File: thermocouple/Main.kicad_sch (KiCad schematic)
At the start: 17 parts, among them IC701 MCP9600, M701 BM15C, SW701 Join, X701 Debug, X702 Thermocouple

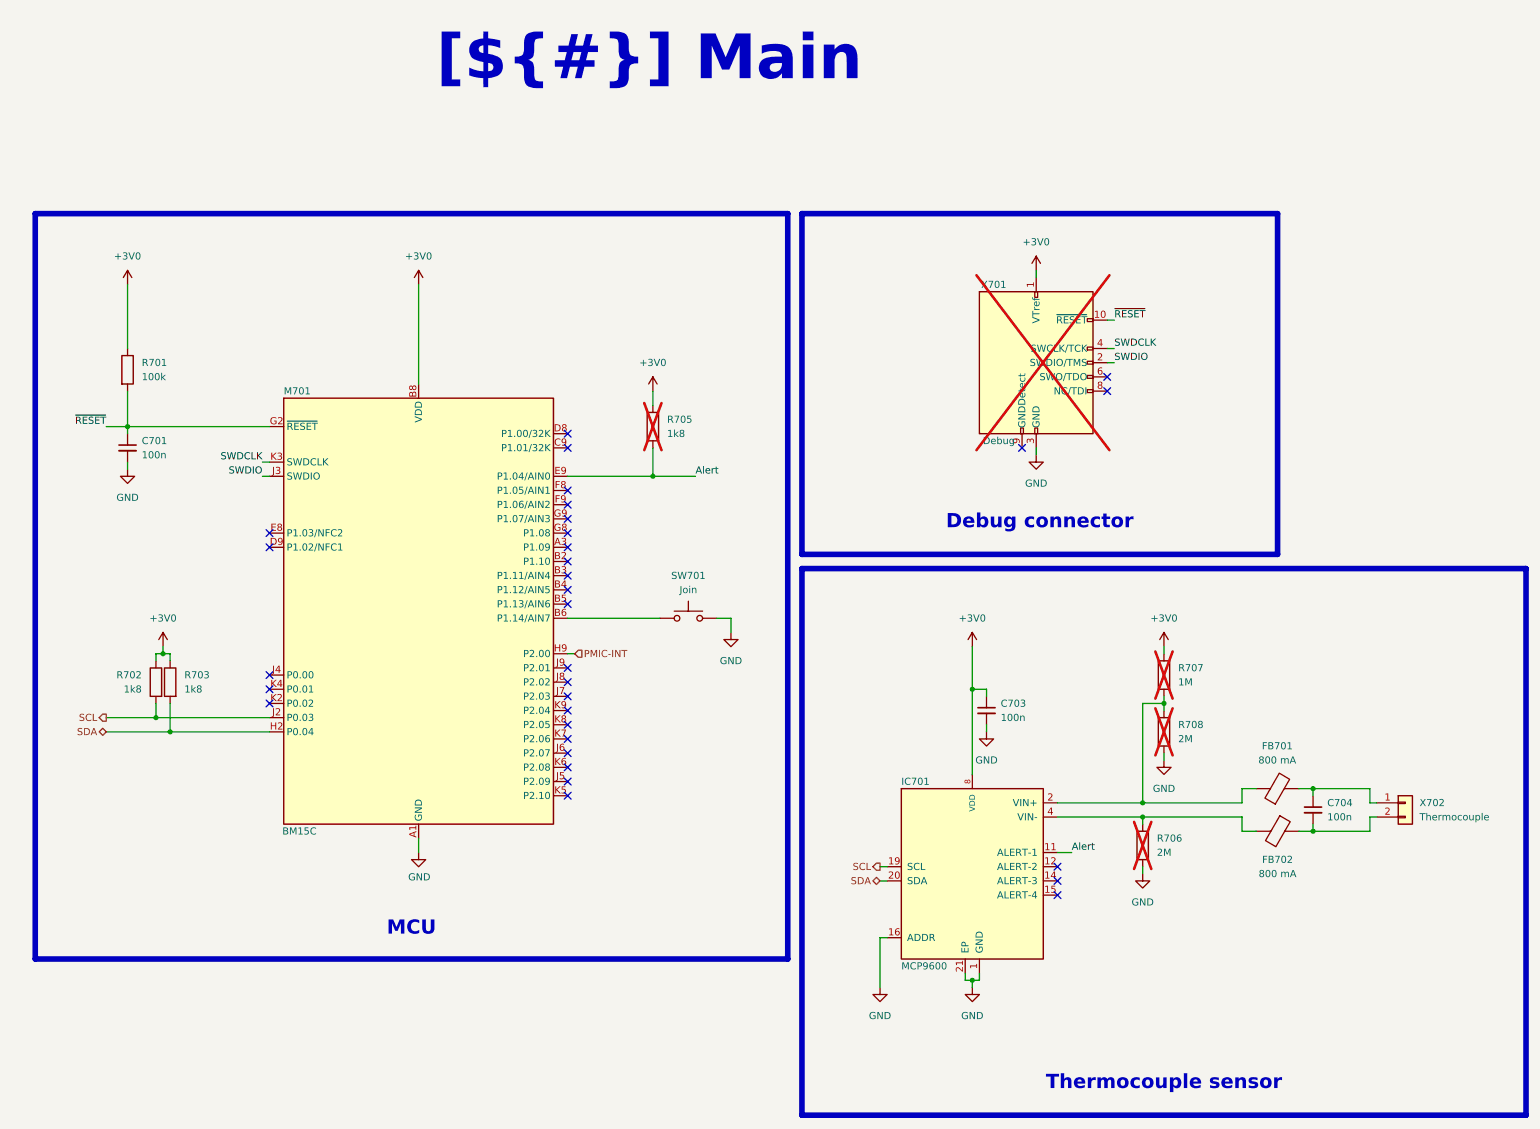
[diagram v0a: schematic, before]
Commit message: CI/CD improvements, fixing broken PMIC-INT
- Update CI/CD to the latest version
- Move PMIC-INT to port 0 to make it usable

Signed-off-by: Daniel Kampert <DanielKampert@kampis-elektroecke.de>
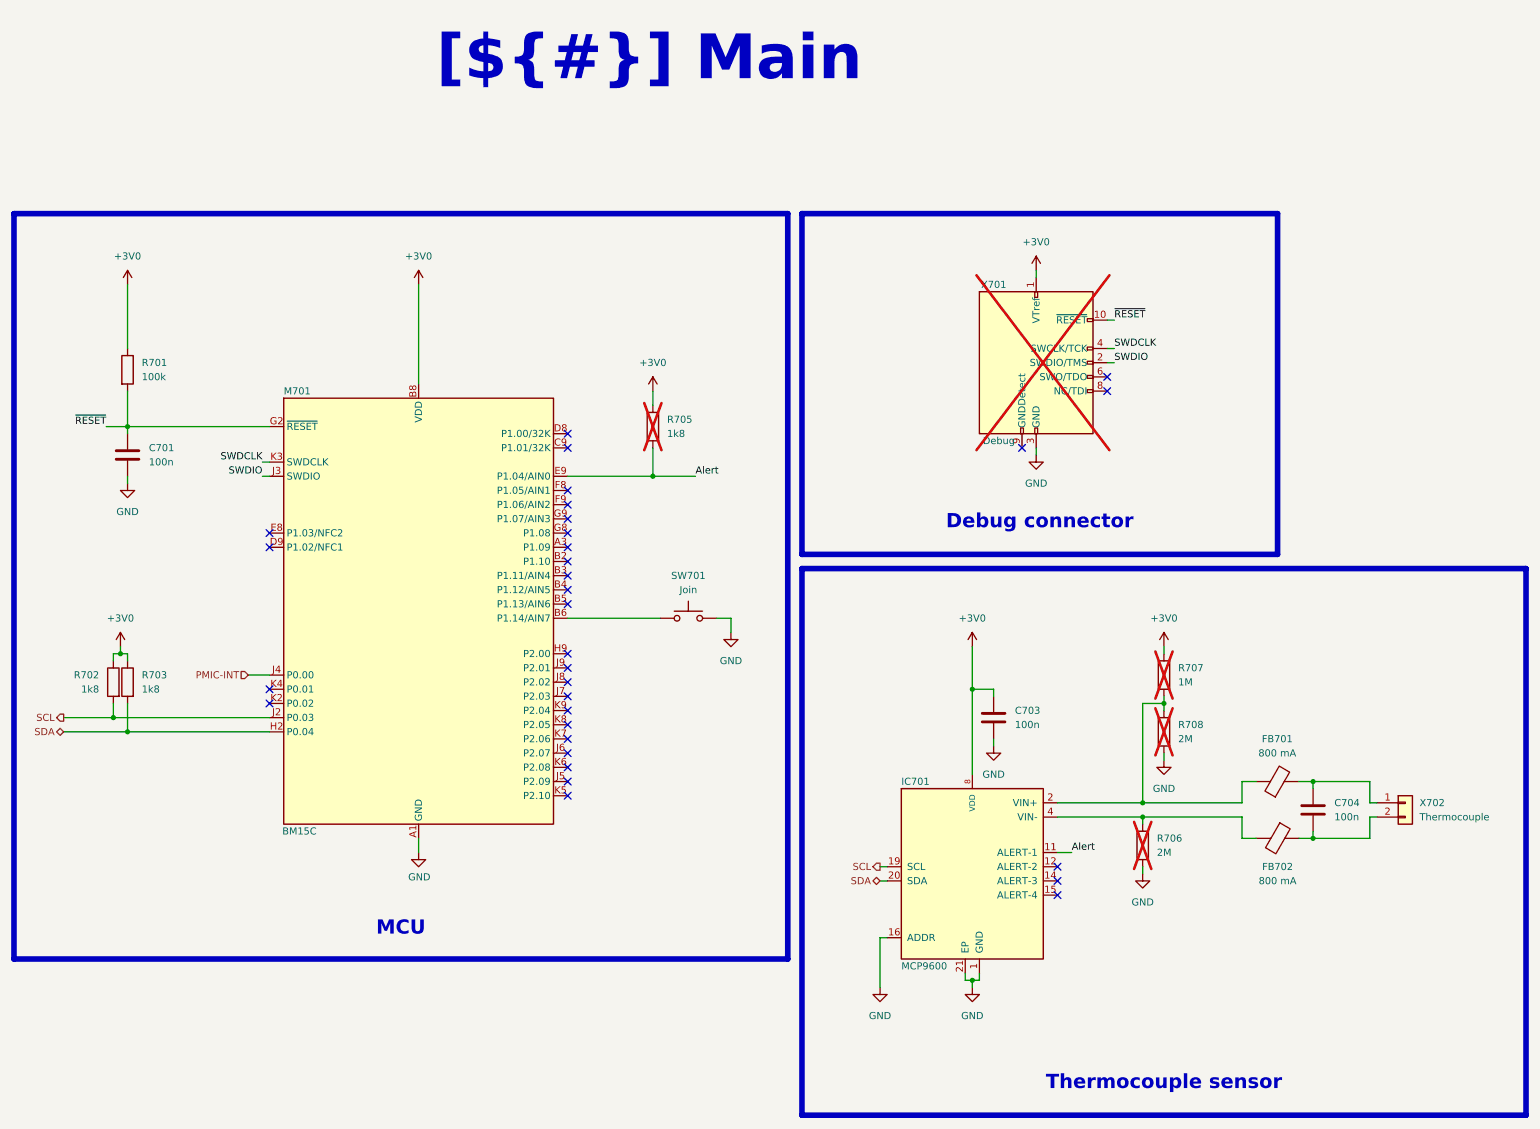
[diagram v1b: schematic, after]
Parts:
- C701, C703, C704: footprint Resistor_SMD:R_0805_2012Metric -> Capacitor_SMD:C_0805_2012Metric; symbol Device:C_Small -> partdb:08055C104K4Z4A; Category (none) -> Kondensator/MLCC; MPN (none) -> 08055C104K4Z4A; Manufacturer (none) -> KYOCERA AVX; Manufacturing Status (none) -> Active; Mass (none) -> 0.006 g; Mouser SPN (none) -> 581-08055C104K4Z4A; Part-DB Footprint (none) -> 0805; Part-DB ID (none) -> 109; Part-DB URL (none) -> https://inventory.lan/de/part/109/info; Stock (none) -> 6; Storage Location (none) -> Sortierregal; manf# 08053F104K4T2A -> 08055C104K4Z4A; mouser# 581-08053F104K4T2A -> 581-08055C104K4Z4A
- M701: symbol Fanstel:BM15C -> partdb:BM15C; Category (none) -> Modul/Fanstel; MPN (none) -> BM15C; Manufacturer (none) -> Fanstel; Manufacturing Status (none) -> Active; Mouser SPN (none) -> 308-BM15C; Part-DB Footprint (none) -> BM15C; Part-DB ID (none) -> 52; Part-DB URL (none) -> https://inventory.lan/de/part/52/info; Stock (none) -> 2; Storage Location (none) -> Sortierregal
- R701: symbol Device:R -> partdb:RT0805FRE13100KL; Category (none) -> Widerstand/Dünnfilmwiderstand; MPN (none) -> RT0805FRE13100KL; Manufacturer (none) -> YAGEO; Manufacturing Status (none) -> Active; Mass (none) -> 0.006 g; Mouser SPN (none) -> 603-RT0805FRE13100KL; Part-DB Footprint (none) -> 0805; Part-DB ID (none) -> 66; Part-DB URL (none) -> https://inventory.lan/de/part/66/info; Stock (none) -> 4; Storage Location (none) -> Sortierregal; manf Bourns -> YAGEO; manf# CR0805-JW-104ELF -> RT0805FRE13100KL; mouser# 652-CR0805-JW-104ELF -> 603-RT0805FRE13100KL
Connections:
- net PMIC-INT: now also M701.J4 (P0.00); no longer M701.H9 (P2.00)
- new net: IC701.10 (NC), IC701.13 (NC), IC701.17 (NC), IC701.18 (NC), IC701.3 (NC), IC701.5 (NC), IC701.6 (NC), IC701.7 (NC), IC701.9 (NC)
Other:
- moved on the sheet: C701, C703, FB701, FB702, R702, R703

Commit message: Change thermocouple connector to a different type
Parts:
- SW701: symbol Switch:SW_Push -> partdb:430182095816; Category (none) -> Bedienelement/Taster; MPN (none) -> 430182095816; Manufacturer (none) -> Wurth Elektronik; Manufacturing Status (none) -> Active; Mass (none) -> 0.26 g; Mouser SPN (none) -> 710-430182095816; Part-DB Footprint (none) -> WS-TASV 6x6; Part-DB ID (none) -> 24; Part-DB URL (none) -> https://inventory.lan/de/part/24/info; Stock (none) -> 0
- X702: footprint TerminalBlock_Phoenix:TerminalBlock_Phoenix_MKDS-1,5-2-5.08_1x02_P5.08mm_Horizontal -> Connector_Phoenix_MC:PhoenixContact_MC_1,5_2-G-3.81_1x02_P3.81mm_Horizontal; manf# 1729128 -> 1803277; mouser# 651-1729128 -> 651-1803277
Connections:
- net GND: now also SW701.4
- net at M701.B6 (P1.14/AIN7), SW701.1: now also SW701.3
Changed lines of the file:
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@@
 	)
 	(junction
+		(at 210.82 123.19)
+		(diameter 0)
+		(color 0 0 0 0)
+	)
+	(junction
 		(at 116.84 143.51)
 		(diameter 0)
@@
 	)
 	(junction
+		(at 224.79 123.19)
+		(diameter 0)
+		(color 0 0 0 0)
+	)
+	(junction
 		(at 328.93 152.4)
 		(diameter 0)
@@
 	(wire
 		(pts
+			(xy 210.82 120.65) (xy 210.82 123.19)
+		)
+		(stroke
+			(width 0)
+			(type default)
+		)
+	)
+	(wire
+		(pts
 			(xy 116.84 138.43) (xy 116.84 143.51)
 		)
@@
 	(wire
 		(pts
+			(xy 222.25 120.65) (xy 224.79 120.65)
+		)
+		(stroke
+			(width 0)
+			(type default)
+		)
+	)
+	(wire
+		(pts
 			(xy 116.84 97.79) (xy 116.84 99.06)
 		)
@@
 	(wire
 		(pts
+			(xy 210.82 123.19) (xy 212.09 123.19)
+		)
+		(stroke
+			(width 0)
+			(type default)
+		)
+	)
+	(wire
+		(pts
 			(xy 210.82 92.71) (xy 210.82 97.79)
 		)
@@
 	(wire
 		(pts
+			(xy 212.09 120.65) (xy 210.82 120.65)
+		)
+		(stroke
+			(width 0)
+			(type default)
+		)
+	)
+	(wire
+		(pts
 			(xy 218.44 97.79) (xy 210.82 97.79)
 		)
@@
 	(wire
 		(pts
-			(xy 195.58 123.19) (xy 212.09 123.19)
+			(xy 195.58 123.19) (xy 210.82 123.19)
 		)
 		(stroke
@@
 		)
 	)
+	(wire
+		(pts
+			(xy 224.79 120.65) (xy 224.79 123.19)
+		)
+		(stroke
+			(width 0)
+			(type default)
+		)
+	)
 	(label "Alert"
 		(at 218.44 97.79 0)
@@
 	)
 	(symbol
-		(lib_id "Switch:SW_Push")
+		(lib_id "partdb:430182095816")
 		(at 217.17 123.19 0)
 		(unit 1)
@@
 		(in_pos_files yes)
 		(dnp no)
+		(fields_autoplaced yes)
 		(property "Reference" "SW701"
-			(at 217.17 115.57 0)
+			(at 217.17 113.03 0)
 			(show_name no)
 			(do_not_autoplace no)
@@
 		)
 		(property "Value" "Join"
-			(at 217.17 118.11 0)
+			(at 217.17 115.57 0)
 			(show_name no)
 			(do_not_autoplace no)
@@
 		)
 		(property "Footprint" "Wuerth:WS-TASV-6x6"
-			(at 217.17 118.11 0)
+			(at 217.17 115.57 0)
 			(hide yes)
 			(show_name no)
@@
 			)
 		)
-		(property "Datasheet" "https://www.we-online.com/components/products/datasheet/430182130816.pdf"
-			(at 217.17 118.11 0)
+		(property "Datasheet" "https://www.we-online.com/components/products/datasheet/430182095816.pdf"
+			(at 217.17 115.57 0)
 			(hide yes)
 			(show_name no)
@@
 			)
 		)
-		(property "Description" "Push button switch, generic, two pins"
+		(property "Description" "Taster 6x6mm 9.5mm 160gf SMD"
 			(at 217.17 123.19 0)
 			(hide yes)
@@
 			)
 		)
+		(property "Config" ""
+			(at 217.17 123.19 0)
+			(hide yes)
+			(show_name no)
+			(do_not_autoplace no)
+			(effects
+				(font
+					(size 1.27 1.27)
+				)
+			)
+		)
+		(property "Part-DB URL" "https://inventory.lan/de/part/24/info"
+			(at 217.17 123.19 0)
+			(hide yes)
+			(show_name no)
+			(do_not_autoplace no)
+			(effects
+				(font
+					(size 1.27 1.27)
+				)
+			)
+		)
+		(property "Category" "Bedienelement/Taster"
+			(at 217.17 123.19 0)
+			(hide yes)
+			(show_name no)
+			(do_not_autoplace no)
+			(effects
+				(font
+					(size 1.27 1.27)
+				)
+			)
+		)
+		(property "Manufacturer" "Wurth Elektronik"
+			(at 217.17 123.19 0)
+			(hide yes)
+			(show_name no)
+			(do_not_autoplace no)
+			(effects
+				(font
+					(size 1.27 1.27)
+				)
+			)
+		)
+		(property "MPN" "430182095816"
+			(at 217.17 123.19 0)
+			(hide yes)
+			(show_name no)
+			(do_not_autoplace no)
+			(effects
+				(font
+					(size 1.27 1.27)
+				)
+			)
+		)
+		(property "Manufacturing Status" "Active"
+			(at 217.17 123.19 0)
+			(hide yes)
+			(show_name no)
+			(do_not_autoplace no)
+			(effects
+				(font
+					(size 1.27 1.27)
+				)
+			)
+		)
+		(property "Part-DB Footprint" "WS-TASV 6x6"
+			(at 217.17 123.19 0)
+			(hide yes)
+			(show_name no)
+			(do_not_autoplace no)
+			(effects
+				(font
+					(size 1.27 1.27)
+				)
+			)
+		)
+		(property "Mass" "0.26 g"
+			(at 217.17 123.19 0)
+			(hide yes)
+			(show_name no)
+			(do_not_autoplace no)
+			(effects
+				(font
+					(size 1.27 1.27)
+				)
+			)
+		)
+		(property "Part-DB ID" "24"
+			(at 217.17 123.19 0)
+			(hide yes)
+			(show_name no)
+			(do_not_autoplace no)
+			(effects
+				(font
+					(size 1.27 1.27)
+				)
+			)
+		)
+		(property "Mouser SPN" "710-430182095816"
+			(at 217.17 123.19 0)
+			(hide yes)
+			(show_name no)
+			(do_not_autoplace no)
+			(effects
+				(font
+					(size 1.27 1.27)
+				)
+			)
+		)
+		(property "Stock" "0"
+			(at 217.17 123.19 0)
+			(hide yes)
+			(show_name no)
+			(do_not_autoplace no)
+			(effects
+				(font
+					(size 1.27 1.27)
+				)
+			)
+		)
 		(pin "2"
 		)
 		(pin "1"
 		)
+		(pin "3"
+		)
+		(pin "4"
+		)
 		(instances
 			(project "Thermocouple"
@@
 			)
 		)
-		(property "Footprint" "TerminalBlock_Phoenix:TerminalBlock_Phoenix_MKDS-1,5-2-5.08_1x02_P5.08mm_Horizontal"
+		(property "Footprint" "Connector_Phoenix_MC:PhoenixContact_MC_1,5_2-G-3.81_1x02_P3.81mm_Horizontal"
 			(at 345.44 156.21 0)
 			(hide yes)
@@
 			)
 		)
-		(property "Datasheet" "https://www.mouser.de/datasheet/3/507/8/phoenix_contact_1729128_en.pdf"
+		(property "Datasheet" "https://www.mouser.de/datasheet/3/507/9/phoenix_contact_1803277_en.pdf"
 			(at 345.44 156.21 0)
 			(hide yes)
@@
 			)
 		)
-		(property "manf#" "1729128"
+		(property "manf#" "1803277"
+			(at 345.44 156.21 0)
+			(hide yes)
+			(show_name no)
+			(do_not_autoplace no)
+			(effects
+				(font
+					(size 1.27 1.27)
+				)
+			)
+		)
+		(property "mouser#" "651-1803277"
 			(at 345.44 156.21 0)
 			(hide yes)
@@
 			)
 		)
-		(property "mouser#" "651-1729128"
+		(property "Config" ""
 			(at 345.44 156.21 0)
 			(hide yes)
